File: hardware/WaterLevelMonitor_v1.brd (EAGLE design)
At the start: 98.7 x 49.5 mm, 55 parts, among them J1 AVR_SPI_PRG_6PTH, J12 D24V5F5, J16 D24V5F5, J17 RJ45, J6 D24V5F5, Q2 2N3904, Q3 NDP6020P, U1 ATMEGA328P_PDIP

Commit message: Add files via upload
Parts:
- removed X1: (no value), con-wago-500:W237-102
- moved J2 2.84 mm to (88.9, 10.2)
- moved J6 1.80 mm to (77.5, 14.0)
- moved J11 1.27 mm to (69.8, 8.89)
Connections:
- net GND: no longer X1.2
- net VBAT: no longer X1.1
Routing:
- net VBAT: track 54.8 -> 46.3 mm
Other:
- board text added: "VBAT"
- board text removed: "+VBAT"
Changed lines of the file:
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@@
 SS1
 SS2</text>
-<text x="73.025" y="10.16" size="1.27" layer="21" font="vector" rot="R270">Battery</text>
+<text x="91.44" y="8.255" size="1.27" layer="21" font="vector" rot="R180">Battery</text>
 <text x="10.795" y="28.575" size="1.27" layer="21" font="vector" rot="R180">SPI</text>
 <wire x1="98.73" y1="49.52" x2="0" y2="49.52" width="0" layer="20"/>
-<text x="75.565" y="0.635" size="3.81" layer="21" font="vector" rot="R90">+</text>
-<text x="48.26" y="0.635" size="1.27" layer="21" font="vector">HW UART</text>
+<text x="85.725" y="11.43" size="3.81" layer="21" font="vector" rot="R90">+</text>
+<text x="46.99" y="0.635" size="1.27" layer="21" font="vector">HW UART</text>
 <text x="34.925" y="0.635" size="1.27" layer="21" font="vector">I2C</text>
 <text x="13.335" y="0.635" size="1.27" layer="21" font="vector">Debug Console</text>
@@
 <text x="50.165" y="37.465" size="1.3208" layer="21" font="vector" distance="90">PD7
 PD6</text>
-<text x="88.265" y="10.795" size="1.27" layer="21" font="vector" rot="R180" align="top-right">+VBAT</text>
+<text x="85.725" y="12.065" size="1.27" layer="21" font="vector" rot="R180" align="top-right">VBAT</text>
 <text x="48.895" y="42.545" size="1.3208" layer="21" font="vector" distance="90">PB0</text>
 </plain>
@@
 <element name="C3" library="SparkFun-Capacitors" package="CAP-PTH-SMALL" value="0.1uF" x="48.26" y="19.05" rot="R90"/>
 <element name="D4" library="SparkFun-DiscreteSemi" package="DIODE-ZENER" value="16V Zener" x="95.25" y="13.335" rot="R270"/>
-<element name="J6" library="SparkFun-Connectors" package="1X04" value="D24V5F5" x="76.2" y="15.24" smashed="yes" rot="R180">
-<attribute name="PROD_ID" value="CONN-09696" x="76.2" y="15.24" size="1.778" layer="27" rot="R180" display="off"/>
-<attribute name="NAME" x="65.9638" y="16.5862" size="1.27" layer="25" ratio="10" rot="R270"/>
-<attribute name="VALUE" x="77.47" y="18.415" size="1.27" layer="27" rot="R180"/>
+<element name="J6" library="SparkFun-Connectors" package="1X04" value="D24V5F5" x="77.47" y="13.97" smashed="yes" rot="R180">
+<attribute name="PROD_ID" value="CONN-09696" x="77.47" y="13.97" size="1.778" layer="27" rot="R180" display="off"/>
+<attribute name="NAME" x="67.2338" y="15.3162" size="1.27" layer="25" ratio="10" rot="R270"/>
+<attribute name="VALUE" x="78.74" y="17.145" size="1.27" layer="27" rot="R180"/>
 </element>
 <element name="Q3" library="transistor-power" package="TO220BV" value="NDP6020P" x="87.63" y="22.86"/>
@@
 <attribute name="NAME" x="65.3034" y="32.4866" size="0.9906" layer="25" ratio="10" rot="R270"/>
 <attribute name="VALUE" x="61.8236" y="32.6136" size="0.9906" layer="27" ratio="10" rot="R270"/>
-</element>
-<element name="X1" library="con-wago-500" package="W237-102" value="" x="80.01" y="7.62">
-<attribute name="OC_NEWARK" value="70K9898" x="80.01" y="7.62" size="1.778" layer="27" display="off"/>
-<attribute name="OC_FARNELL" value="unknown" x="80.01" y="7.62" size="1.778" layer="27" display="off"/>
-<attribute name="MPN" value="237-102" x="80.01" y="7.62" size="1.778" layer="27" display="off"/>
-<attribute name="MF" value="" x="80.01" y="7.62" size="1.778" layer="27" display="off"/>
 </element>
 <element name="U$1" library="SparkFun-Electromechanical" package="STAND-OFF" value="" x="7.62" y="3.81"/>
@@
 <attribute name="VALUE" x="59.69" y="5.715" size="1.27" layer="27"/>
 </element>
-<element name="J11" library="SparkFun-Connectors" package="1X02" value="" x="68.58" y="8.89" smashed="yes">
-<attribute name="NAME" x="66.7512" y="7.5438" size="1.27" layer="25" ratio="10" rot="R90"/>
-<attribute name="VALUE" x="67.31" y="5.715" size="1.27" layer="27"/>
+<element name="J11" library="SparkFun-Connectors" package="1X02" value="" x="69.85" y="8.89" smashed="yes">
+<attribute name="NAME" x="68.0212" y="7.5438" size="1.27" layer="25" ratio="10" rot="R90"/>
+<attribute name="VALUE" x="68.58" y="5.715" size="1.27" layer="27"/>
 </element>
 <element name="J13" library="SparkFun-Connectors" package="1X03" value="" x="22.225" y="19.685" smashed="yes" rot="R90">
@@
 <attribute name="VALUE" x="25.4" y="18.415" size="1.27" layer="27" rot="R90"/>
 </element>
-<element name="J2" library="SparkFun-Connectors" package="1X02" value="" x="91.44" y="8.89" smashed="yes" rot="R180">
-<attribute name="NAME" x="85.6488" y="9.6012" size="1.27" layer="25" ratio="10" rot="R270"/>
-<attribute name="VALUE" x="92.71" y="12.065" size="1.27" layer="27" rot="R180"/>
+<element name="J2" library="SparkFun-Connectors" package="1X02" value="" x="88.9" y="10.16" smashed="yes" rot="R180">
+<attribute name="NAME" x="83.1088" y="11.5062" size="1.27" layer="25" ratio="10" rot="R270"/>
+<attribute name="VALUE" x="90.17" y="13.335" size="1.27" layer="27" rot="R180"/>
 </element>
 <element name="J4" library="SparkFun-Connectors" package="1X02_NO_SILK" value="" x="41.91" y="43.18" smashed="yes">
@@
 <signals>
 <signal name="GND">
-<contactref element="X1" pad="2"/>
 <contactref element="Q2" pad="1"/>
 <contactref element="R5" pad="1"/>
@@
 </signal>
 <signal name="VBAT">
-<contactref element="X1" pad="1"/>
 <contactref element="Q3" pad="S"/>
 <contactref element="R2" pad="2"/>
@@
 <contactref element="J6" pad="2"/>
 <contactref element="JP1" pad="1"/>
-<wire x1="77.51" y1="6.35" x2="73.66" y2="10.2" width="0.6096" layer="16"/>
-<wire x1="73.66" y1="10.2" x2="73.66" y2="15.24" width="0.6096" layer="16"/>
 <wire x1="95.25" y1="16.891" x2="90.551" y2="17.145" width="0.6096" layer="16"/>
 <wire x1="90.551" y1="17.145" x2="90.17" y2="17.145" width="0.6096" layer="16"/>
-<wire x1="73.66" y1="15.24" x2="73.66" y2="15.875" width="0.6096" layer="1"/>
-<wire x1="73.66" y1="15.875" x2="71.755" y2="17.78" width="0.6096" layer="1"/>
-<wire x1="71.755" y1="17.78" x2="69.85" y2="17.78" width="0.6096" layer="1"/>
-<wire x1="69.85" y1="17.78" x2="68.58" y2="19.05" width="0.6096" layer="1"/>
 <wire x1="68.58" y1="19.05" x2="68.58" y2="20.955" width="0.6096" layer="1"/>
 <wire x1="68.58" y1="20.955" x2="66.04" y2="22.86" width="0.6096" layer="1"/>
 <wire x1="66.04" y1="22.86" x2="66.04" y2="24.315" width="0.6096" layer="1"/>
 <wire x1="90.17" y1="20.32" x2="90.17" y2="17.145" width="1.27" layer="16"/>
-<wire x1="90.17" y1="17.145" x2="84.7725" y2="11.7475" width="1.27" layer="16"/>
-<wire x1="84.7725" y1="11.7475" x2="83.185" y2="10.16" width="1.27" layer="16"/>
-<wire x1="83.185" y1="10.16" x2="81.28" y2="10.16" width="1.27" layer="16"/>
-<wire x1="81.28" y1="10.16" x2="77.51" y2="6.39" width="1.27" layer="16"/>
-<wire x1="77.51" y1="6.39" x2="77.51" y2="6.35" width="1.27" layer="16"/>
 <contactref element="J2" pad="2"/>
-<wire x1="88.9" y1="8.89" x2="86.0425" y2="11.7475" width="0.4064" layer="16"/>
-<wire x1="86.0425" y1="11.7475" x2="84.7725" y2="11.7475" width="0.4064" layer="16"/>
+<wire x1="86.36" y1="10.16" x2="86.36" y2="12.7" width="0.8128" layer="16"/>
+<wire x1="86.36" y1="12.7" x2="90.17" y2="16.51" width="0.8128" layer="16"/>
+<wire x1="90.17" y1="16.51" x2="90.17" y2="17.145" width="0.8128" layer="16"/>
+<wire x1="68.58" y1="19.05" x2="69.85" y2="17.78" width="0.6096" layer="1"/>
+<wire x1="69.85" y1="17.78" x2="72.39" y2="17.78" width="0.6096" layer="1"/>
+<wire x1="72.39" y1="17.78" x2="74.93" y2="15.24" width="0.6096" layer="1"/>
+<wire x1="74.93" y1="15.24" x2="74.93" y2="13.97" width="0.6096" layer="1"/>
+<wire x1="74.93" y1="13.97" x2="74.93" y2="12.7" width="0.6096" layer="16"/>
+<wire x1="74.93" y1="12.7" x2="77.47" y2="10.16" width="0.6096" layer="16"/>
+<wire x1="77.47" y1="10.16" x2="86.36" y2="10.16" width="0.6096" layer="16"/>
 </signal>
 <signal name="N$2">
@@
 <wire x1="69.85" y1="31.75" x2="69.85" y2="22.86" width="0.4064" layer="16"/>
 <wire x1="69.85" y1="22.86" x2="68.58" y2="21.59" width="0.4064" layer="16"/>
-<wire x1="68.58" y1="21.59" x2="68.58" y2="19.05" width="0.4064" layer="16"/>
-<wire x1="68.58" y1="19.05" x2="66.04" y2="16.51" width="0.4064" layer="16"/>
-<wire x1="66.04" y1="16.51" x2="66.04" y2="13.97" width="0.4064" layer="16"/>
-<wire x1="66.04" y1="13.97" x2="64.77" y2="12.7" width="0.4064" layer="16"/>
 <wire x1="64.77" y1="12.7" x2="63.5" y2="12.7" width="0.4064" layer="16"/>
 <wire x1="63.5" y1="12.7" x2="60.96" y2="10.16" width="0.4064" layer="16"/>
@@
 <wire x1="22.225" y1="24.765" x2="19.05" y2="24.765" width="0.4064" layer="16"/>
 <wire x1="15.24" y1="5.08" x2="15.24" y2="2.54" width="0.4064" layer="16"/>
+<wire x1="64.77" y1="12.7" x2="68.58" y2="16.51" width="0.4064" layer="16"/>
+<wire x1="68.58" y1="16.51" x2="68.58" y2="21.59" width="0.4064" layer="16"/>
 </signal>
 <signal name="N$15">
@@
 <contactref element="J6" pad="4"/>
 <contactref element="J11" pad="1"/>
-<wire x1="68.58" y1="8.89" x2="68.58" y2="15.24" width="0.4064" layer="16"/>
+<wire x1="69.85" y1="8.89" x2="69.85" y2="13.97" width="0.4064" layer="16"/>
 <wire x1="63.5" y1="15.24" x2="63.5" y2="24.13" width="0.254" layer="16"/>
 <wire x1="63.5" y1="24.13" x2="62.23" y2="25.4" width="0.254" layer="16"/>
@@
 <wire x1="58.42" y1="42.291" x2="60.325" y2="44.196" width="0.254" layer="16"/>
 <wire x1="63.5" y1="15.24" x2="54.61" y2="6.35" width="0.4064" layer="16"/>
-<wire x1="68.58" y1="15.24" x2="63.5" y2="15.24" width="0.4064" layer="1"/>
+<wire x1="69.85" y1="13.97" x2="63.5" y2="15.24" width="0.4064" layer="1"/>
 <wire x1="48.26" y1="3.81" x2="48.26" y2="6.35" width="0.4064" layer="16"/>
 <wire x1="33.02" y1="3.81" x2="33.02" y2="6.35" width="0.4064" layer="16"/>

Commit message: Add files via upload
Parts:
- moved C4 2.54 mm to (55.2, 29.2)
- moved C5 2.54 mm to (55.2, 34.3)
- moved Q1 1.91 mm to (48.3, 31.8)
- moved D1 1.27 mm to (59.7, 14.0)
- moved D2 1.27 mm to (21.6, 12.7)
- moved C1 0.64 mm to (61.0, 19.7)
- moved C2 0.64 mm to (53.3, 19.7)
- moved C3 0.64 mm to (48.3, 18.4)
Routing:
- net VBATSW: track 38.0 -> 72.1 mm
- net VCEL: track 46.3 -> 78.3 mm
- net N$31: track 6.50 -> 35.2 mm
- net N$29: track 7.14 -> 29.0 mm
- net N$34: track 8.41 -> 20.4 mm
- net VBAT: track 46.3 -> 58.0 mm
- net N$7: track 37.3 -> 40.3 mm
- net N$4: track 40.2 -> 43.2 mm
- net N$9: track 11.3 -> 13.9 mm
- net N$10: track 11.3 -> 13.9 mm
- net N$20: track 12.0 -> 10.7 mm
- net VMCU: track 40.7 -> 41.6 mm
- net N$22: track 19.6 -> 18.8 mm
- net N$21: track 5.08 -> 5.61 mm
- net N$32: track 33.7 -> 34.2 mm
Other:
- board text added: "Out Gnd In Shd"

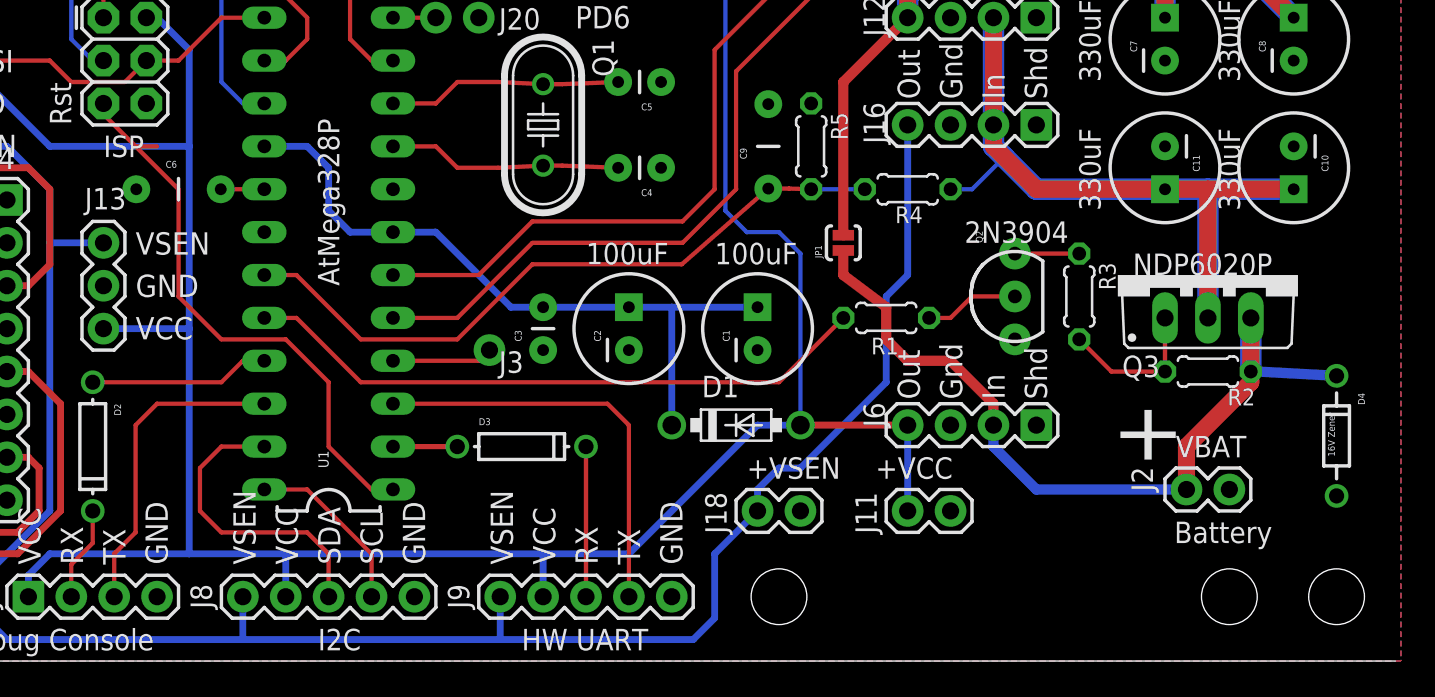
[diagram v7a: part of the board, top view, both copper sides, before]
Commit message: added DC power jack
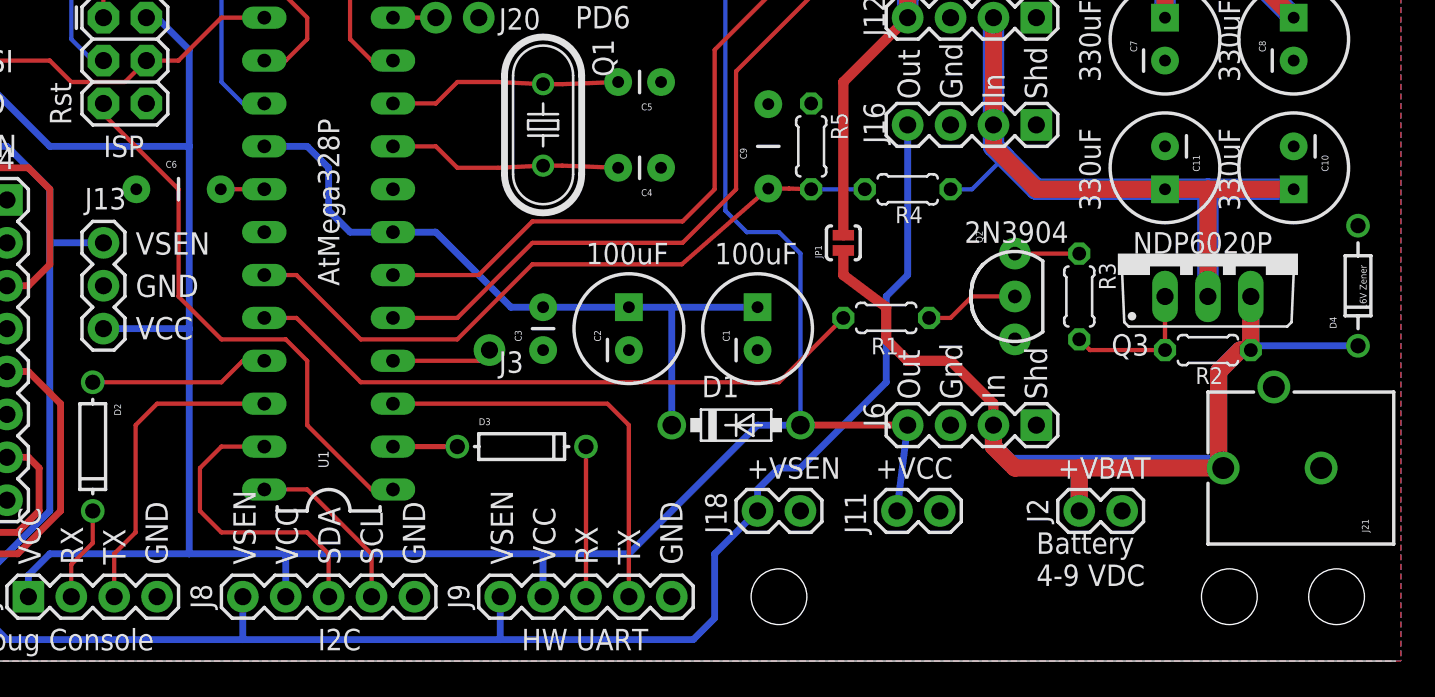
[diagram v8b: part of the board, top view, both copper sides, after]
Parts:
- added J21: POWER_JACKPTH_BREAD, SparkFun-Connectors:POWER_JACK_PTH_BREAD
- moved J2 8.98 mm to (80.0, 8.89), turned to 0 degrees
- moved D4 8.98 mm to (96.5, 22.2), turned to 90 degrees
- moved Q3 1.27 mm to (87.6, 24.1)
- moved R2 1.27 mm to (87.6, 18.4)
- moved J11 0.63 mm to (69.2, 8.89)
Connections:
- net GND: now also J2.2, J21.GND; no longer J2.1
- net VBAT: now also J2.1, J21.PWR; no longer J2.2
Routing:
- net VBAT: track 58.0 -> 80.4 mm
- net VBATSW: track 72.1 -> 69.6 mm
- net N$32: track 34.2 -> 32.9 mm
- net N$2: track 9.04 -> 8.52 mm
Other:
- board text added: "+VBAT"
- board text added: "Battery 4-9 VDC"
- board text removed: "+"
- board text removed: "Battery"
- board text removed: "VBAT"
